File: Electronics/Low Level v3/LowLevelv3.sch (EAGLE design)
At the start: 58 parts, among them IC2 MCP4802, K1 ORWH-SH-105D1F,000, K3 ORWH-SH-105D1F,000, Q1 16MHz, T1 2N3904, T2 2N3904, U1 284512-4, U4 MCP2515, U5 MCP2551DIL08, X3 Motor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

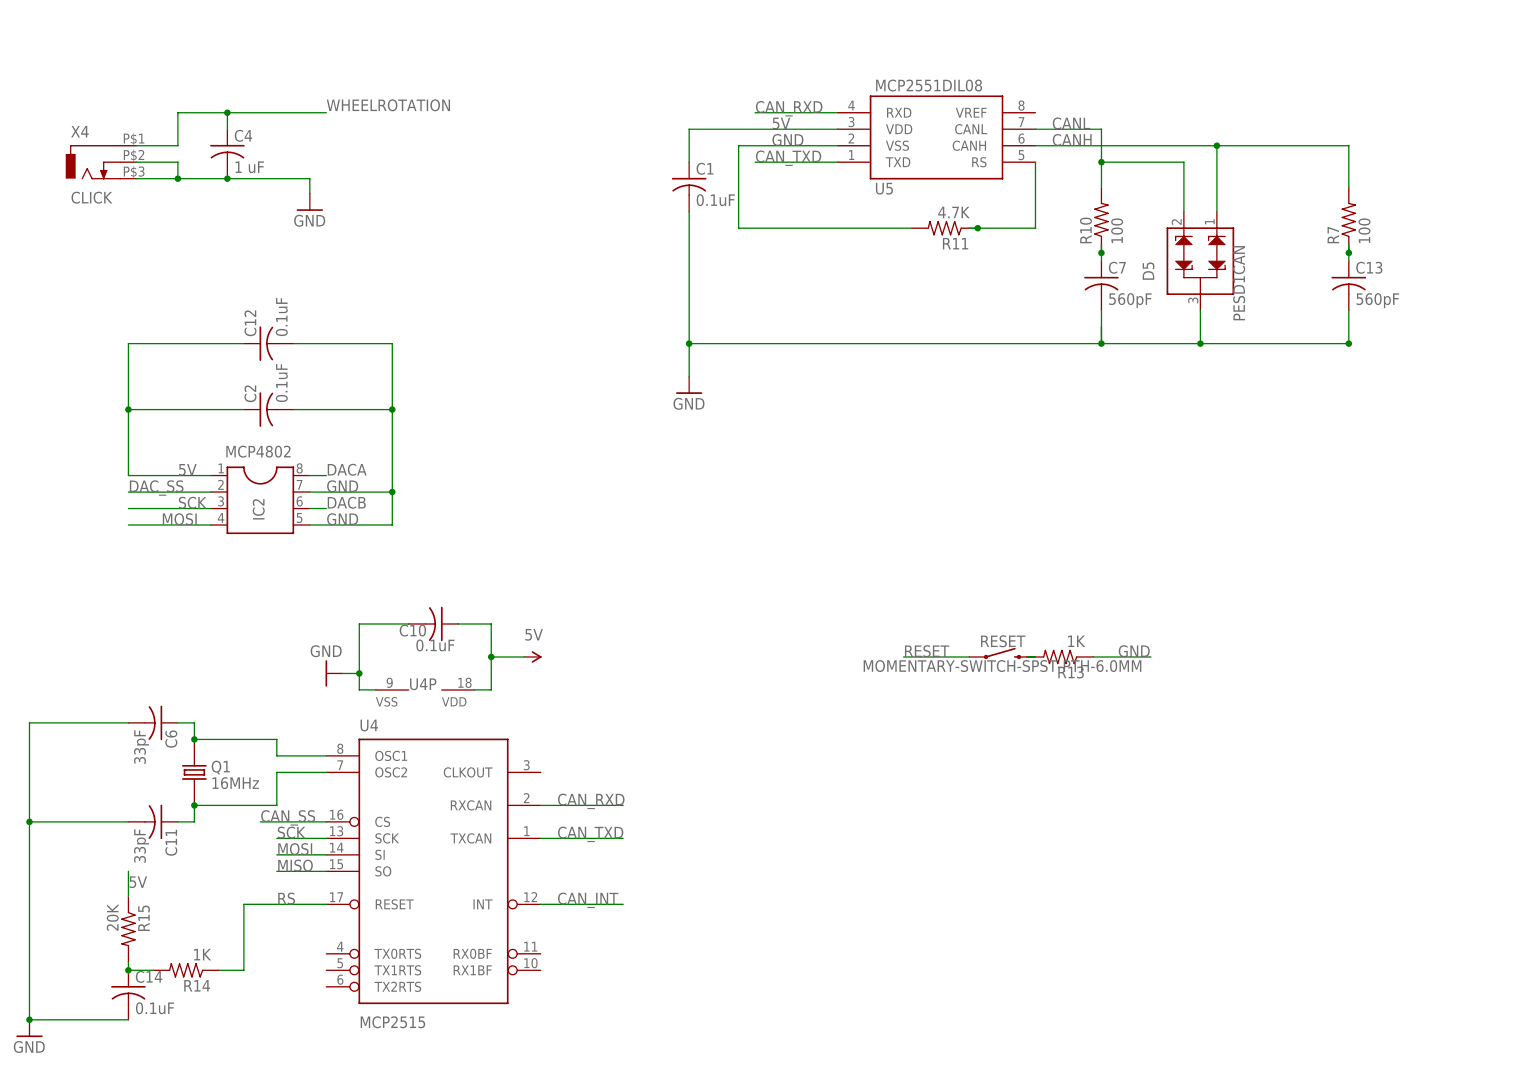
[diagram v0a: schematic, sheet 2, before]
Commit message: Added e-stop, routed additional connetions to DB15, changed board layout
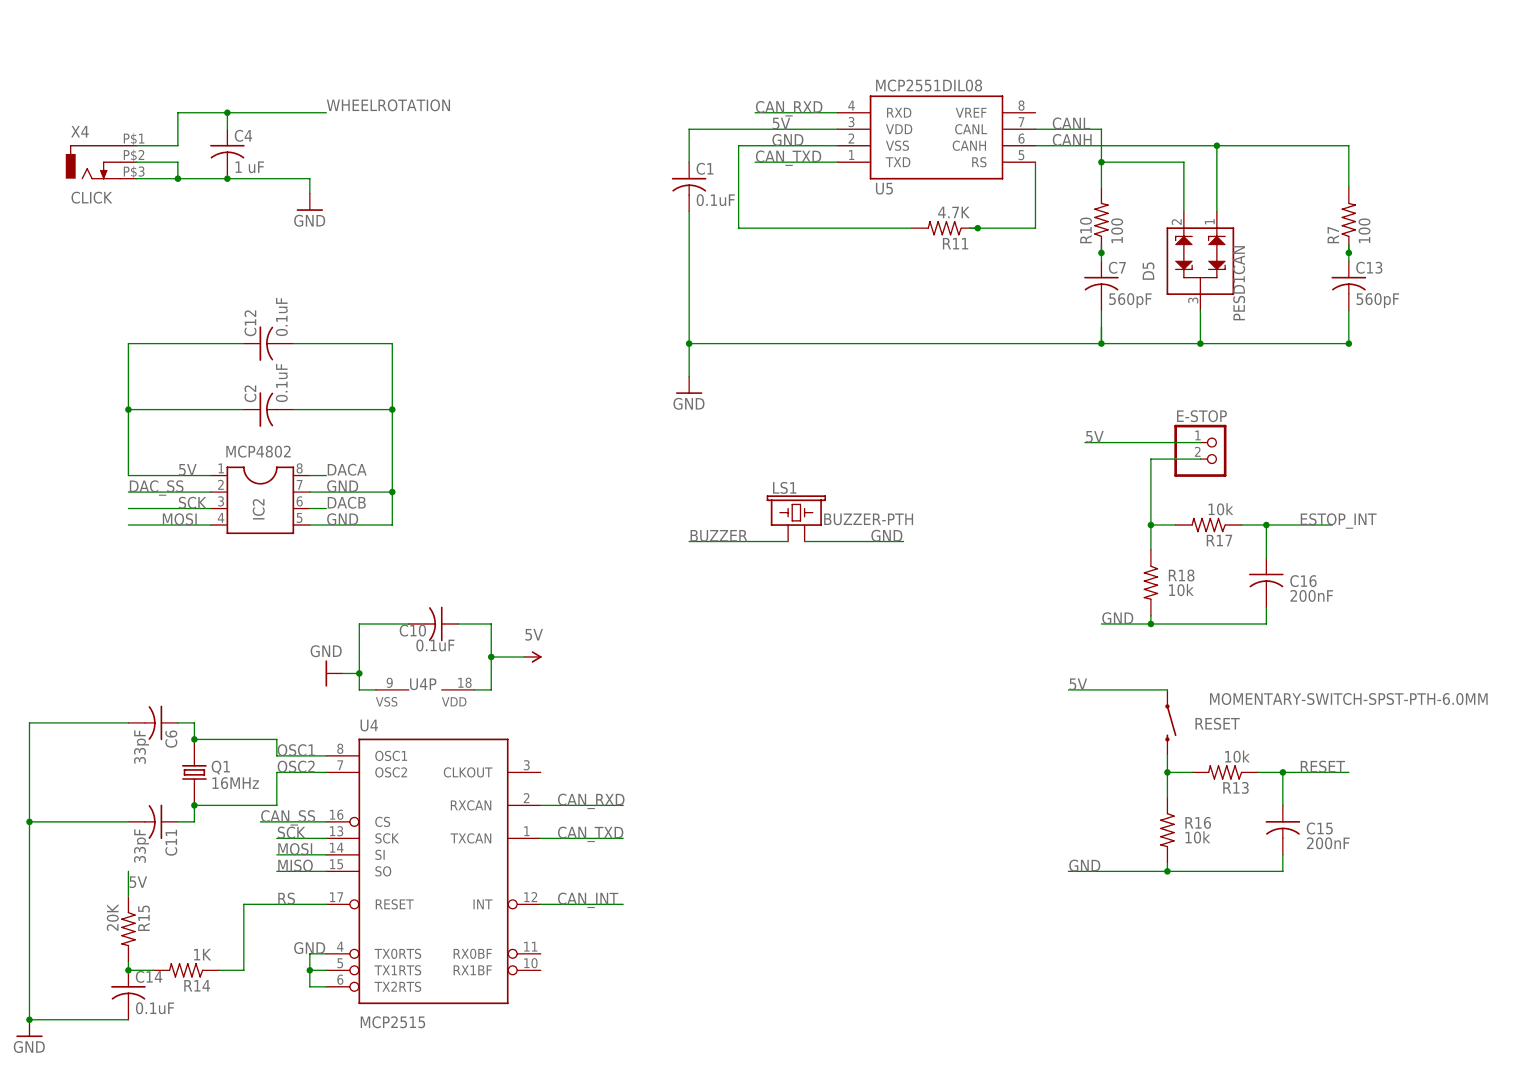
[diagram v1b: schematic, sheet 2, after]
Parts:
- added C15, C16: 200nF, resistor:C-USC1206
- added E-STOP: (no value), pinhead:PINHD-1X2
- added LS1: BUZZER-PTH, SparkFun-Electromechanical:BUZZER-PTH
- added R16, R17, R18: 10k, resistor:R-US_R1206
- R13: value 1K -> 10k
- renumbered J1 to CAN_HEADER
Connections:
- net N$17 renamed OSC1
- net N$18 renamed OSC2
- removed net STR_L: ADCL.6
- removed net STR_R: ADCL.5
- new net BRAKE_PWM: DIGITAL_0-7.3, X3.1
- new net BUZZER: LS1.1, MEGA_EXPANSION.18
- new net D_36: MEGA_EXPANSION.20, X3.7
- new net ESTOP_INT: C16.1, DIGITAL_0-7.4, R17.1, X3.6
- new net N$8: E-STOP.2, R17.2, R18.1
- new net REGEN_ACTIVE: MEGA_EXPANSION.34, X3.5
- new net RX0: DIGITAL_0-7.1
- new net TX0: DIGITAL_0-7.2
- net 5V: now also E-STOP.1, RESET.1
- net GND: now also C15.2, C16.2, LS1.2, R16.2, R18.2, U4>NAME.TX0RTS, U4>NAME.TX1RTS, U4>NAME.TX2RTS; no longer R13.1
- net L_SENSE: now also ADCL.6
- net N$1: now also R16.1
- net RESET: now also C15.1, R13.1; no longer RESET.1
- net REVERSE: now also X3.4
- net R_SENSE: now also ADCL.5
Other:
- moved on the sheet: D1, R13, RESET, U1

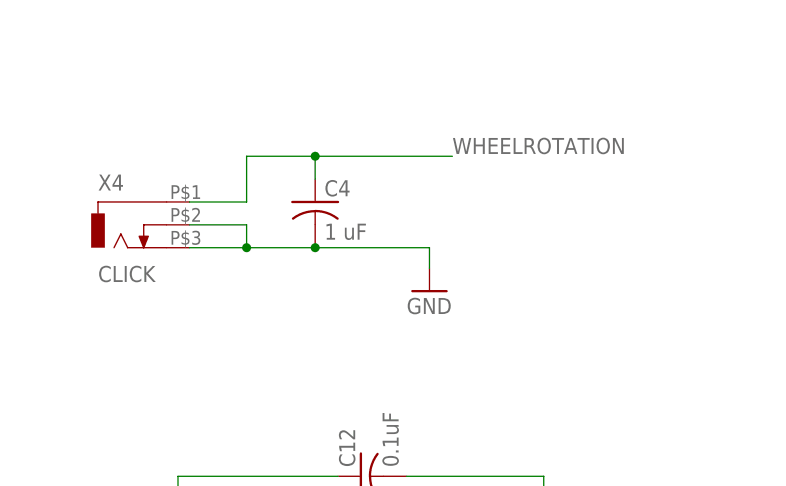
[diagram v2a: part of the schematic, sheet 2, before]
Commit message: Updates to board, schematic, library
added 4.7k pullup to odometer and took first steps towards replacing the arduino headers with custom component with correct pin names.
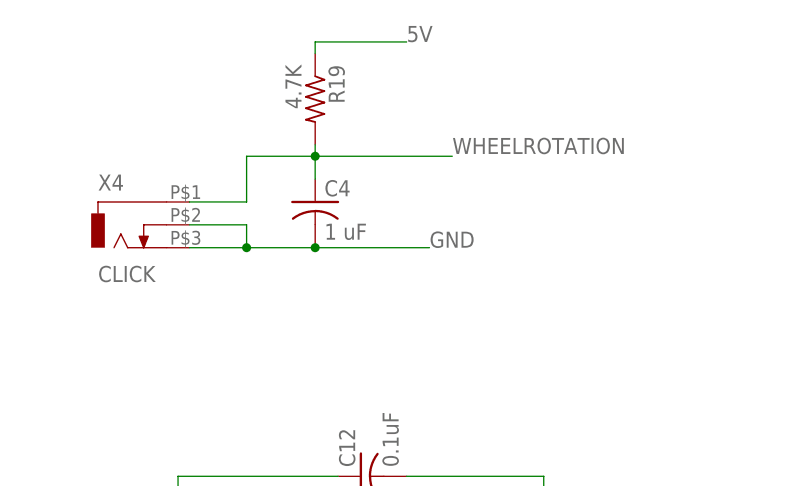
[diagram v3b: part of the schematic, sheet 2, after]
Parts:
- added R19: 4.7K, resistor:R-US_R1206
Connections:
- net 5V: now also R19.1
- net WHEELROTATION: now also R19.2
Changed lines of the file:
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@@
 <drawing>
 <settings>
-<setting alwaysvectorfont="no"/>
+<setting alwaysvectorfont="yes"/>
 <setting keepoldvectorfont="yes"/>
 <setting verticaltext="up"/>
@@
 <part name="C9" library="resistor" library_urn="urn:adsk.eagle:library:348" deviceset="C-US" device="C1206" package3d_urn="urn:adsk.eagle:package:23618/2" value="1 uF"/>
 <part name="DIGITAL_8-13" library="pinhead" library_urn="urn:adsk.eagle:library:325" deviceset="PINHD-1X8" device="" package3d_urn="urn:adsk.eagle:package:22409/2" value="Digital 8-13"/>
-<part name="GND5" library="supply1" library_urn="urn:adsk.eagle:library:371" deviceset="GND" device=""/>
 <part name="P+10" library="SparkFun-Aesthetics" library_urn="urn:adsk.eagle:library:507" deviceset="5V" device="">
 <attribute name="SPICEPREFIX" value="G"/>
@@
 <part name="R18" library="resistor" library_urn="urn:adsk.eagle:library:348" deviceset="R-US_" device="R1206" package3d_urn="urn:adsk.eagle:package:23540/2" value="10k"/>
 <part name="C16" library="resistor" library_urn="urn:adsk.eagle:library:348" deviceset="C-US" device="C1206" package3d_urn="urn:adsk.eagle:package:23618/2" value="200nF"/>
+<part name="R19" library="resistor" library_urn="urn:adsk.eagle:library:348" deviceset="R-US_" device="R1206" package3d_urn="urn:adsk.eagle:package:23540/2" value="4.7K"/>
 </parts>
 <sheets>
@@
 <attribute name="VALUE" x="31.75" y="140.97" size="1.778" layer="96"/>
 </instance>
-<instance part="GND5" gate="1" x="68.58" y="139.954" smashed="yes">
-<attribute name="VALUE" x="66.04" y="137.414" size="1.778" layer="96"/>
-</instance>
 <instance part="P+10" gate="G$1" x="101.6" y="71.12" smashed="yes" rot="R270">
 <attribute name="VALUE" x="101.6" y="73.66" size="1.778" layer="96"/>
@@
 <attribute name="NAME" x="219.456" y="81.915" size="1.778" layer="95"/>
 <attribute name="VALUE" x="219.456" y="79.629" size="1.778" layer="96"/>
+</instance>
+<instance part="R19" gate="G$1" x="55.88" y="161.29" smashed="yes" rot="R270">
+<attribute name="NAME" x="57.3786" y="165.1" size="1.778" layer="95" rot="R270"/>
+<attribute name="VALUE" x="52.578" y="165.1" size="1.778" layer="96" rot="R270"/>
 </instance>
 </instances>
@@
 <label x="187.96" y="104.14" size="1.778" layer="95"/>
 </segment>
+<segment>
+<pinref part="R19" gate="G$1" pin="1"/>
+<wire x1="55.88" y1="166.37" x2="55.88" y2="167.64" width="0.1524" layer="91"/>
+<wire x1="55.88" y1="167.64" x2="66.04" y2="167.64" width="0.1524" layer="91"/>
+<label x="66.04" y="167.64" size="1.778" layer="95"/>
+</segment>
 </net>
 <net name="GND" class="1">
-<segment>
-<pinref part="C4" gate="G$1" pin="2"/>
-<wire x1="48.26" y1="144.78" x2="55.88" y2="144.78" width="0.1524" layer="91"/>
-<junction x="55.88" y="144.78"/>
-<pinref part="X4" gate="G$1" pin="3"/>
-<wire x1="48.26" y1="147.32" x2="48.26" y2="144.78" width="0.1524" layer="91"/>
-<wire x1="48.26" y1="144.78" x2="41.91" y2="144.78" width="0.1524" layer="91"/>
-<pinref part="X4" gate="G$1" pin="2"/>
-<wire x1="41.91" y1="147.32" x2="48.26" y2="147.32" width="0.1524" layer="91"/>
-<junction x="48.26" y="144.78"/>
-<pinref part="GND5" gate="1" pin="GND"/>
-<wire x1="68.58" y1="144.78" x2="68.58" y2="142.494" width="0.1524" layer="91"/>
-<wire x1="55.88" y1="144.78" x2="68.58" y2="144.78" width="0.1524" layer="91"/>
-</segment>
 <segment>
 <pinref part="IC2" gate="G$1" pin="5"/>
@@
 <label x="66.04" y="25.4" size="1.778" layer="95"/>
 </segment>
+<segment>
+<pinref part="C4" gate="G$1" pin="2"/>
+<wire x1="48.26" y1="144.78" x2="55.88" y2="144.78" width="0.1524" layer="91"/>
+<junction x="55.88" y="144.78"/>
+<pinref part="X4" gate="G$1" pin="3"/>
+<wire x1="48.26" y1="147.32" x2="48.26" y2="144.78" width="0.1524" layer="91"/>
+<wire x1="48.26" y1="144.78" x2="41.91" y2="144.78" width="0.1524" layer="91"/>
+<pinref part="X4" gate="G$1" pin="2"/>
+<wire x1="41.91" y1="147.32" x2="48.26" y2="147.32" width="0.1524" layer="91"/>
+<junction x="48.26" y="144.78"/>
+<wire x1="55.88" y1="144.78" x2="68.58" y2="144.78" width="0.1524" layer="91"/>
+<label x="68.58" y="144.78" size="1.778" layer="95"/>
+</segment>
 </net>
 <net name="DAC_SS" class="3">
@@
 <wire x1="55.88" y1="154.94" x2="55.88" y2="152.4" width="0.1524" layer="91"/>
 <junction x="55.88" y="154.94"/>
-</segment>
-</net>
+<pinref part="R19" gate="G$1" pin="2"/>
+<wire x1="55.88" y1="156.21" x2="55.88" y2="154.94" width="0.1524" layer="91"/>
+</segment>
+</net>
